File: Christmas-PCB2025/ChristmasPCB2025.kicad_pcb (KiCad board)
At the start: 2 copper layers, 76.2 x 93.3 mm, 30 parts, among them Q1 2N7002_C306856, U1 ESP32-C3_SUPERMINI_TH

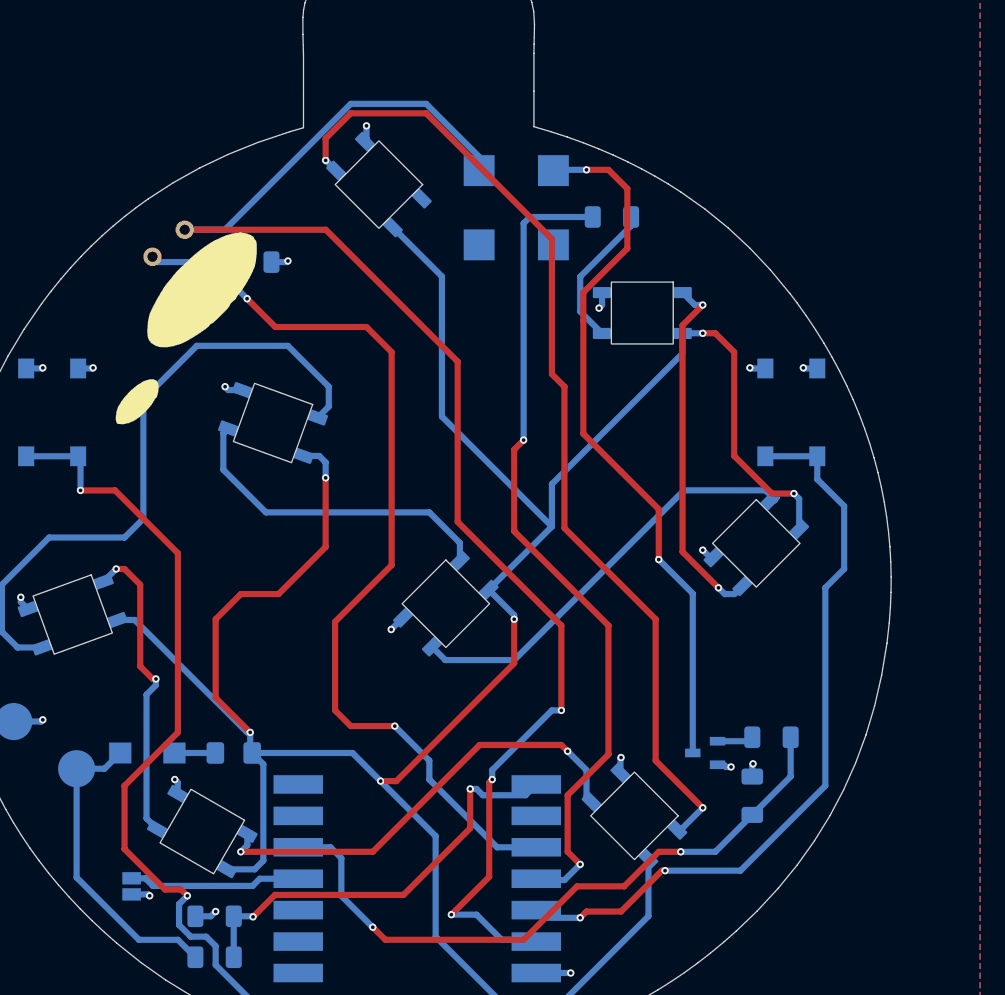
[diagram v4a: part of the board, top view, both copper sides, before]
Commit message: finished silkscreen
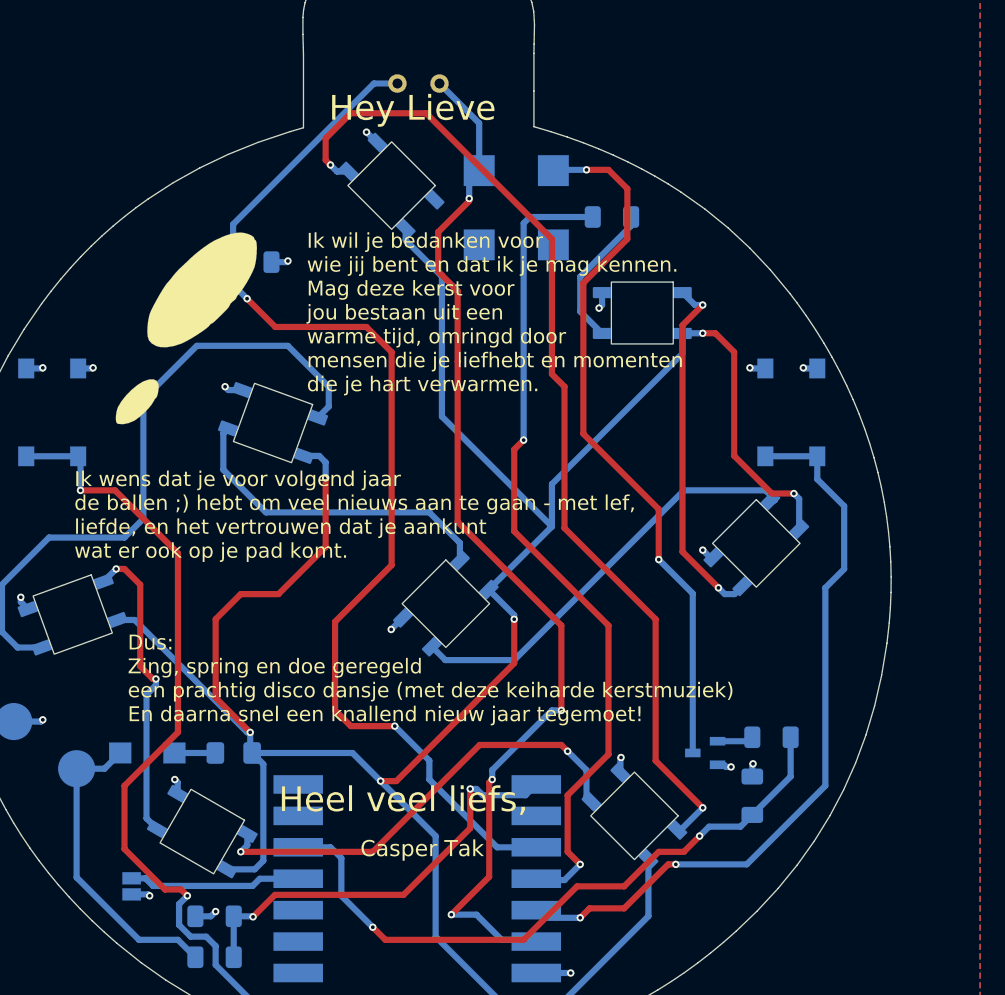
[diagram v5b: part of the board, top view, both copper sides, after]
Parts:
- moved LDR1 23.7 mm to (145.6, 71.0), turned to 180 degrees
- moved LED8 1.03 mm to (141.7, 79.2)
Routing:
- net +3V3: track 117.4 -> 85.9 mm, vias 3 -> 4
- net Net-(U1-GPIO2): track 76.2 -> 90.5 mm
- net Net-(LED7-DOUT): track 80.1 -> 81.2 mm
- net +5V: track 212.4 -> 211.9 mm
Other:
- board text added: "Casper Tak"
- board text added: "Christmas_PCB V1.0 27-07-2025 Casper R. Tak"
- board text added: "Dus: Zing, spring en doe geregeld een prachtig disco dansje (met deze keiharde kerstmuziek) En daarna snel een knallend nieuw jaar tegemoet!"
- board text added: "Heel veel liefs,"
- board text added: "Hey Lieve"
- board text added: "Ik wens dat je voor volgend jaar de ballen ;) hebt om veel nieuws aan te gaan - met lef, liefde, en het vertrouwen dat je aankunt wat er ook op je pad komt."
- board text added: "Ik wil je bedanken voor wie jij bent en dat ik je mag kennen. Mag deze kerst voor jou bestaan uit een warme tijd, omringd door mensen die je liefhebt en momenten die je hart verwarmen."
- board text added: "Voeding: AAA batterijen en/of USB-C ->"

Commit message: Design production files
this was ordered
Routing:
- net GND: track 29.6 -> 34.5 mm
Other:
- board text added: "Dus: Zing, spring en doe geregeld een prachtig disco dansje (op deze keiharde kerstmuziek) En straks snel een knallend nieuw jaar tegemoet!"
- board text removed: "Dus: Zing, spring en doe geregeld een prachtig disco dansje (met deze keiharde kerstmuziek) En daarna snel een knallend nieuw jaar tegemoet!"
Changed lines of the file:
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@@
 		(layer "Edge.Cuts")
 	)
-	(gr_text "Dus:\nZing, spring en doe geregeld \neen prachtig disco dansje (met deze keiharde kerstmuziek) \nEn daarna snel een knallend nieuw jaar tegemoet!"
+	(gr_text "Dus:\nZing, spring en doe geregeld \neen prachtig disco dansje (op deze keiharde kerstmuziek) \nEn straks snel een knallend nieuw jaar tegemoet!"
 		(at 120.396 122.682 0)
 		(layer "F.SilkS")
@@
 	)
 	(via
-		(at 175.006 93.98)
+		(at 176.6 95.5)
 		(size 0.6)
 		(drill 0.3)
@@
 	)
 	(via
-		(at 122.174 136.652)
+		(at 118.8 133.1)
 		(size 0.6)
 		(drill 0.3)
@@
 	)
 	(via
-		(at 113.538 93.98)
-		(size 0.6)
-		(drill 0.3)
-		(layers "F.Cu" "B.Cu")
-		(net 1)
-	)
-	(via
-		(at 156.21 142.891649)
-		(size 0.6)
-		(drill 0.3)
-		(layers "F.Cu" "B.Cu")
-		(net 1)
-	)
-	(segment
-		(start 156.21 142.891649)
-		(end 153.421915 142.891649)
-		(width 0.5)
-		(layer "B.Cu")
+		(at 111.7 95.4)
+		(size 0.6)
+		(drill 0.3)
+		(layers "F.Cu" "B.Cu")
+		(net 1)
+	)
+	(via
+		(at 150.5 141.3)
+		(size 0.6)
+		(drill 0.3)
+		(layers "F.Cu" "B.Cu")
 		(net 1)
 	)
@@
 	)
 	(segment
-		(start 175.054771 94.028771)
-		(end 175.006 93.98)
-		(width 0.5)
-		(layer "B.Cu")
-		(net 1)
-	)
-	(segment
 		(start 117.553229 94.028771)
 		(end 117.602 93.98)
@@
 	)
 	(segment
+		(start 152.091649 142.891649)
+		(end 153.421915 142.891649)
+		(width 0.5)
+		(layer "B.Cu")
+		(net 1)
+	)
+	(segment
 		(start 116.395777 94.028771)
 		(end 117.553229 94.028771)
@@
 	)
 	(segment
-		(start 120.715777 136.538771)
-		(end 122.060771 136.538771)
+		(start 111.7 95.4)
+		(end 111.7 94.524548)
 		(width 0.5)
 		(layer "B.Cu")
@@
 	)
 	(segment
-		(start 113.489229 94.028771)
-		(end 113.538 93.98)
-		(width 0.5)
-		(layer "B.Cu")
-		(net 1)
-	)
-	(segment
 		(start 171.933277 94.028771)
 		(end 170.736771 94.028771)
@@
 	)
 	(segment
+		(start 111.7 94.524548)
+		(end 112.195777 94.028771)
+		(width 0.5)
+		(layer "B.Cu")
+		(net 1)
+	)
+	(segment
 		(start 111.190777 122.568771)
 		(end 109.079229 122.568771)
@@
 	)
 	(segment
+		(start 176.6 94.495494)
+		(end 176.133277 94.028771)
+		(width 0.5)
+		(layer "B.Cu")
+		(net 1)
+	)
+	(segment
 		(start 128.542713 95.776713)
 		(end 128.27 95.504)
@@
 	)
 	(segment
-		(start 112.195777 94.028771)
-		(end 113.489229 94.028771)
+		(start 120.366777 136.189771)
+		(end 120.715777 136.538771)
 		(width 0.5)
 		(layer "B.Cu")
@@
 	)
 	(segment
+		(start 150.5 141.3)
+		(end 152.091649 142.891649)
+		(width 0.5)
+		(layer "B.Cu")
+		(net 1)
+	)
+	(segment
 		(start 170.880777 126.045223)
 		(end 170.942 125.984)
@@
 	)
 	(segment
-		(start 176.133277 94.028771)
-		(end 175.054771 94.028771)
+		(start 176.6 95.5)
+		(end 176.6 94.495494)
+		(width 0.5)
+		(layer "B.Cu")
+		(net 1)
+	)
+	(segment
+		(start 118.8 135.7)
+		(end 119.289771 136.189771)
+		(width 0.5)
+		(layer "B.Cu")
+		(net 1)
+	)
+	(segment
+		(start 119.289771 136.189771)
+		(end 120.366777 136.189771)
 		(width 0.5)
 		(layer "B.Cu")
@@
 	)
 	(segment
-		(start 122.060771 136.538771)
-		(end 122.174 136.652)
-		(width 0.5)
-		(layer "B.Cu")
-		(net 1)
-	)
-	(segment
 		(start 125.870777 138.308771)
 		(end 127.121229 138.308771)
@@
 	)
 	(segment
+		(start 118.8 133.1)
+		(end 118.8 135.7)
+		(width 0.5)
+		(layer "B.Cu")
+		(net 1)
+	)
+	(segment
 		(start 140.553177 75.783177)
 		(end 139.7 74.93)
@@
 	)
 	(segment
+		(start 145.5 86.2)
+		(end 145.5 83)
+		(width 0.5)
+		(layer "F.Cu")
+		(net 2)
+	)
+	(segment
+		(start 147.066 87.766)
+		(end 145.5 86.2)
+		(width 0.5)
+		(layer "F.Cu")
+		(net 2)
+	)
+	(segment
 		(start 146.558 138.176)
 		(end 149.617 135.117)
@@
 	)
 	(segment
-		(start 147.066 87.766)
-		(end 145.8 86.5)
-		(width 0.5)
-		(layer "F.Cu")
-		(net 2)
-	)
-	(segment
-		(start 145.8 86.5)
-		(end 145.5 86.2)
-		(width 0.5)
-		(layer "F.Cu")
-		(net 2)
-	)
-	(segment
-		(start 147.066 93.472)
+		(start 147.066 106.426)
+		(end 147.066 87.766)
+		(width 0.5)
+		(layer "F.Cu")
+		(net 2)
+	)
+	(segment
+		(start 155.448 114.808)
 		(end 147.066 106.426)
 		(width 0.5)
@@
 	)
 	(segment
-		(start 147.066 106.426)
+		(start 145.5 83)
+		(end 148 80.5)
+		(width 0.5)
+		(layer "F.Cu")
+		(net 2)
+	)
+	(segment
+		(start 155.448 121.2)
 		(end 155.448 114.808)
+		(width 0.5)
+		(layer "F.Cu")
+		(net 2)
+	)
+	(segment
+		(start 149.617 127.497)
+		(end 149.86 127.254)
 		(width 0.5)
 		(layer "F.Cu")
@@
 	)
 	(segment
-		(start 155.448 114.808)
-		(end 155.448 121.666)
-		(width 0.5)
-		(layer "F.Cu")
-		(net 2)
-	)
-	(segment
-		(start 145.5 83)
-		(end 148 80.5)
-		(width 0.5)
-		(layer "F.Cu")
-		(net 2)
-	)
-	(segment
-		(start 149.617 127.497)
-		(end 149.86 127.254)
-		(width 0.5)
-		(layer "F.Cu")
-		(net 2)
-	)
-	(segment
 		(start 149.617 135.117)
 		(end 149.617 127.497)
@@
 		(net 2)
 	)
-	(segment
-		(start 147.066 93.472)
-		(end 147.066 87.766)
-		(width 0.5)
-		(layer "F.Cu")
-		(net 2)
-	)
-	(segment
-		(start 145.5 86.2)
-		(end 145.5 83)
-		(width 0.5)
-		(layer "F.Cu")
-		(net 2)
-	)
-	(via
-		(at 155.448 121.666)
+	(via
+		(at 155.448 121.2)
 		(size 0.6)
 		(drill 0.3)
@@
 	)
 	(segment
+		(start 149.86 126.788)
+		(end 149.86 127.254)
+		(width 0.5)
+		(layer "B.Cu")
+		(net 2)
+	)
+	(segment
 		(start 148 80.3)
 		(end 148 78.845148)
@@
 	)
 	(segment
-		(start 149.86 126.492)
-		(end 154.686 121.666)
-		(width 0.5)
-		(layer "B.Cu")
-		(net 2)
-	)
-	(segment
-		(start 149.86 127.254)
-		(end 149.86 126.492)
-		(width 0.5)
-		(layer "B.Cu")
-		(net 2)
-	)
-	(segment
 		(start 145.6 71)
 		(end 148.805377 74.205377)
@@
 	)
 	(segment
+		(start 155.448 121.2)
+		(end 149.86 126.788)
+		(width 0.5)
+		(layer "B.Cu")
+		(net 2)
+	)
+	(segment
 		(start 148.805377 74.205377)
 		(end 148.805377 78.039771)
 		(width 0.5)
 		(layer "B.Cu")
-		(net 2)
-	)
-	(segment
-		(start 154.686 121.666)
-		(end 155.448 121.666)
-		(width 0.5)
-		(layer "B.Cu")

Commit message: working on code and fixed button design error.
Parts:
- removed BATT+: ~, TestPoint:TestPoint_Pad_D3.0mm
- removed BATT-: TestPoint_Alt, TestPoint:TestPoint_Pad_D3.0mm
- removed BATTPACK1:: Batteryplaceholder, MountingHole:MountingHole_2.1mm
- removed G***: LOGO, project_footprints:ornament_shadow
- removed G***: LOGO, project_footprints:ornament_crown
- removed G***: LOGO, project_footprints:ornament_reflect
- removed REF**: MountingHole_2.5mm, idlehands_footprints:MountingHole_2.5mm_NO
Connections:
- BUTTON1 pad 2: GND -> Net-(U1-GPIO4)
- BUTTON1 pad 3: Net-(U1-GPIO4) -> GND
- BUTTON2 pad 2: GND -> Net-(U1-GPIO5)
- BUTTON2 pad 3: Net-(U1-GPIO5) -> GND
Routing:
- net GND: track 34.5 -> 45.8 mm, vias 20 -> 18
- net Net-(U1-GPIO5): track 65.2 -> 68.1 mm
- net Net-(U1-GPIO4): track 60.4 -> 63.3 mm
